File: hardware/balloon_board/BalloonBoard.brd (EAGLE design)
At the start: 64.4 x 71.1 mm, 35 parts, among them IC1 TLC274P, J1 Com 4, J2 Com 3, J3 22-27-2021-02

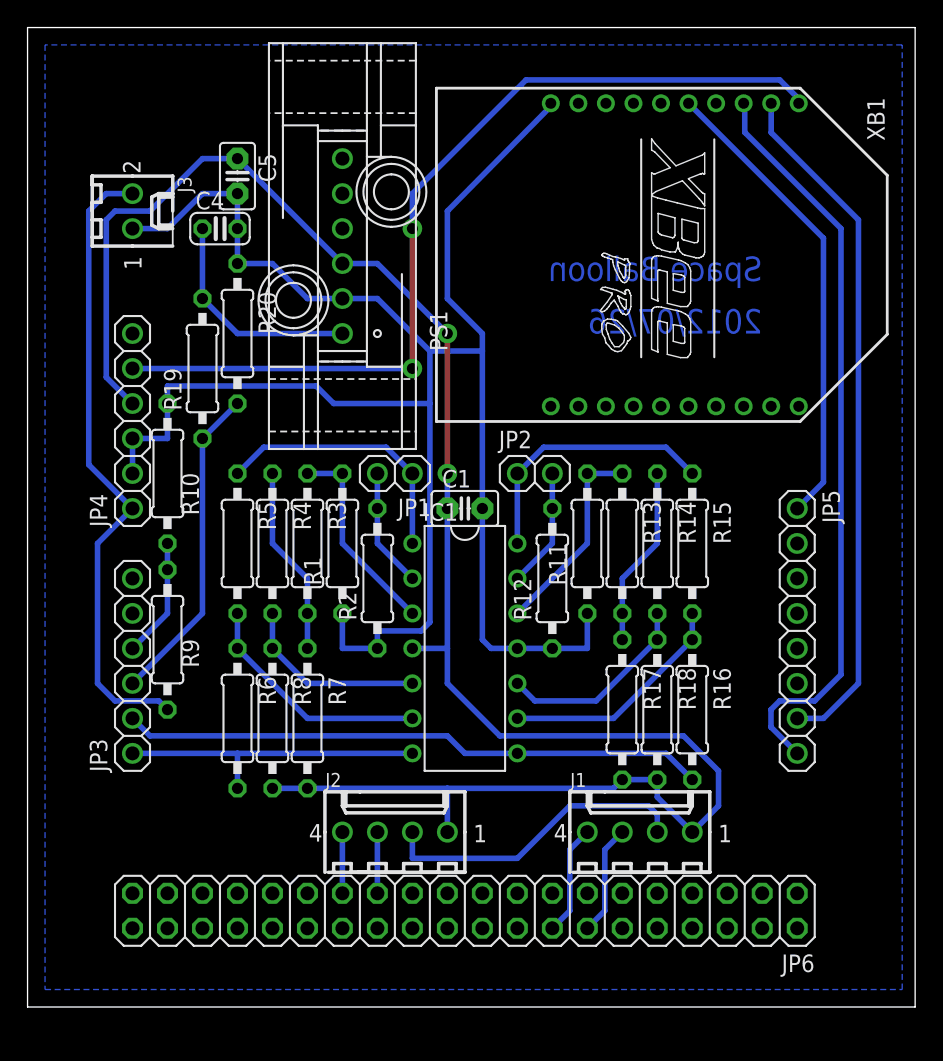
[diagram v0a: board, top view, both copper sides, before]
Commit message: new layout with gyro and pressure sensor
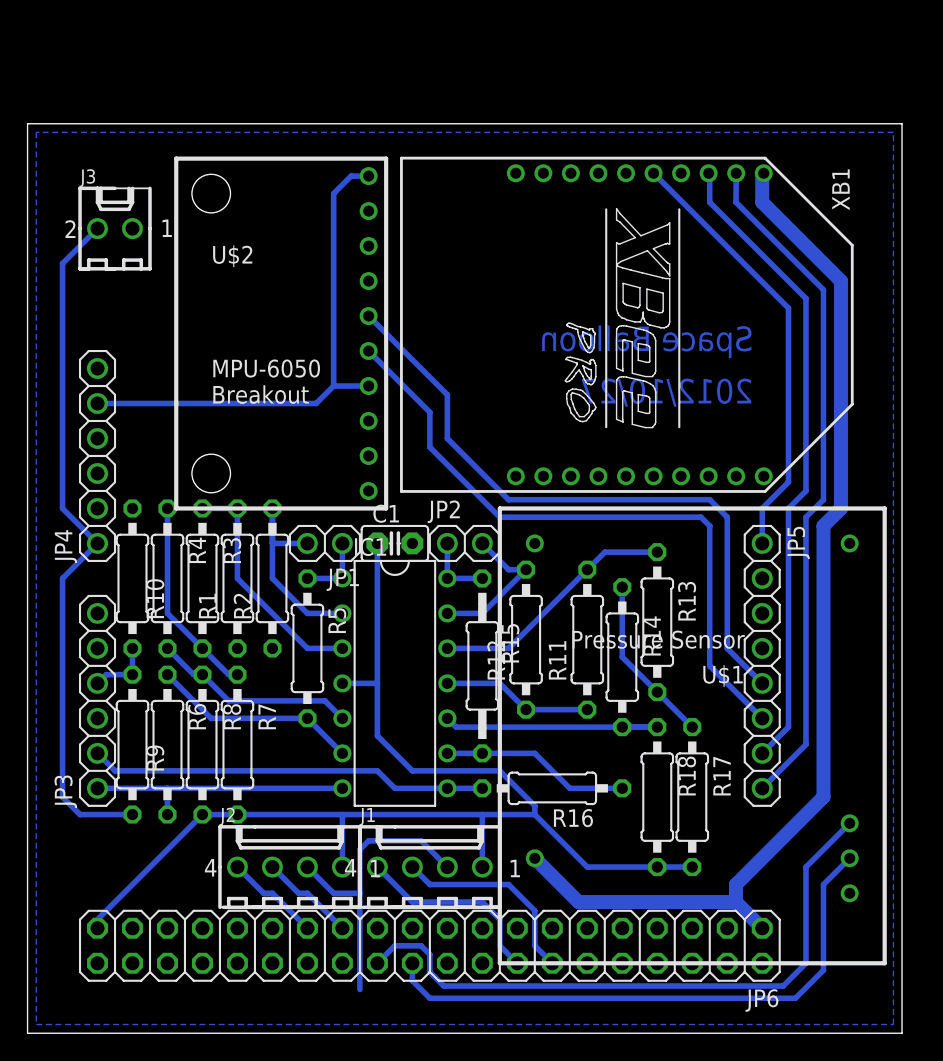
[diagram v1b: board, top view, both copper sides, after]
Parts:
- removed C4: 470p, resistor:C025-024X044
- removed C5: 10n, capacitor-wima:C2.5-2
- removed PS1: MPX5100DP, mpx-freescale:867C-V
- removed R19: 22k, resistor:0207/10
- removed R20: 68k, resistor:0207/10
- added U$1: PRESSUREMODULE, SpaceBallonV3:DIL24
- added U$2: MPU-6050, SpaceBallonV3:MPU-6050_BREAKOUT
- R15: device resistor:0207/10 -> resistor:0207/12
- moved R15 17.6 mm to (33.0, 26.7)
- moved J1 15.5 mm to (29.2, 12.1)
- moved R16 11.7 mm to (38.1, 17.8), turned to 180 degrees
- moved R5 9.16 mm to (20.3, 27.9)
- moved R14 8.64 mm to (43.2, 27.3)
- moved R17 8.13 mm to (48.3, 17.1)
- moved J2 8.03 mm to (19.1, 12.1)
- moved R9 8.03 mm to (7.62, 21.0)
- moved R1 8.03 mm to (15.2, 33.0)
- moved R3 8.03 mm to (12.7, 33.0)
- moved R4 8.03 mm to (10.2, 33.0)
- moved R10 8.03 mm to (7.62, 33.0)
- moved R2 7.62 mm to (17.8, 33.0)
- moved JP1 7.18 mm to (21.6, 35.6)
- moved JP2 7.18 mm to (31.8, 35.6)
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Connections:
- new net +3V3_B: JP4.5, U$2.10, U$2.4
- new net N$26: JP6.22, U$1.3
- new net N$27: JP6.24, U$1.4
- net +3V3: now also JP6.1, U$1.22; no longer JP4.5
- net +5V: now also JP6.39; no longer C5.1, JP4.4, PS1.3
- net GND: now also JP6.38, U$1.13, U$1.2, U$2.9; no longer C4.2, C5.2, PS1.2, R20.1
- net N$17: now also JP5.8; no longer JP5.7
- net N$18: now also JP5.7; no longer JP5.8
- net N$20: now also JP5.6, U$2.5; no longer JP3.3, R19.1, R20.2
- net N$25: now also JP5.5, U$2.6; no longer C4.1, PS1.1, R19.2
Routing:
- net GND: track 169.1 -> 33.1 mm
- net +5V: track 137.7 -> 86.8 mm, vias 2 -> 0
- net N$27: track 0.00 -> 45.8 mm
- net N$26: track 0.00 -> 41.4 mm
- net +3V3_B: track 0.00 -> 37.2 mm
- net N$25: track 16.3 -> 47.1 mm
- net N$20: track 23.5 -> 47.1 mm
- net N$6: track 19.4 -> 5.08 mm
- net N$14: track 19.4 -> 5.08 mm
- net N$16: track 42.5 -> 29.0 mm
- net +3V3: track 65.4 -> 77.2 mm, vias 2 -> 0
- net N$18: track 54.5 -> 46.3 mm
- net N$1: track 8.67 -> 16.3 mm
- net N$21: track 8.04 -> 14.5 mm
- net N$22: track 8.04 -> 14.2 mm
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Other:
- board size 64.4 x 71.1 mm -> 63.5 x 66 mm
- board text added: "2012/10/27"
- board text removed: "2012/07/26"
